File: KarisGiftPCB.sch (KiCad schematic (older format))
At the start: 43 parts

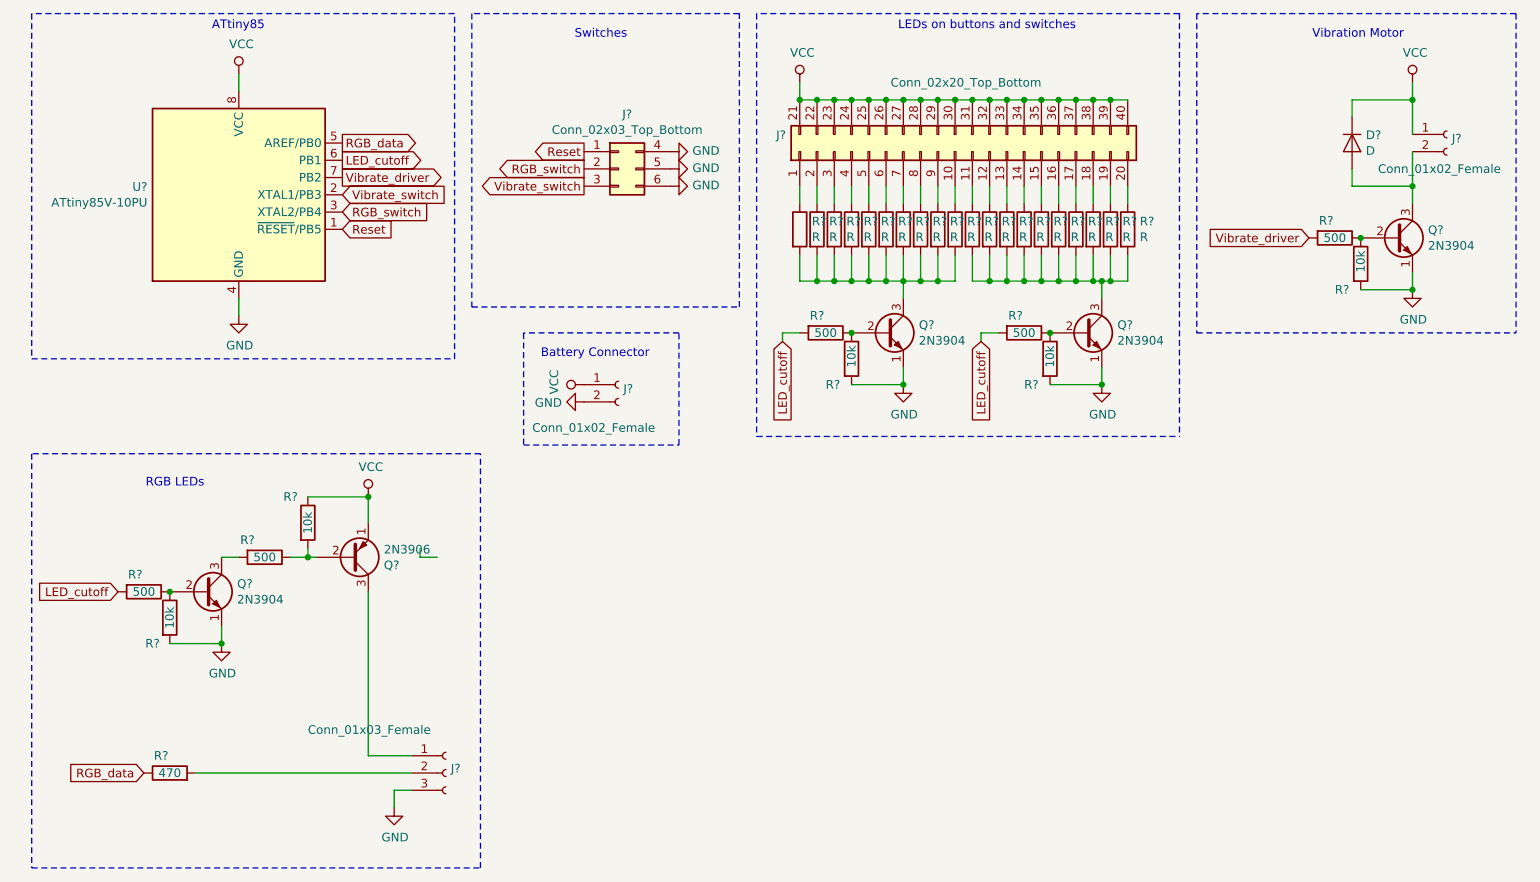
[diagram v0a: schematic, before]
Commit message: Added footprints to all parts in schematic.
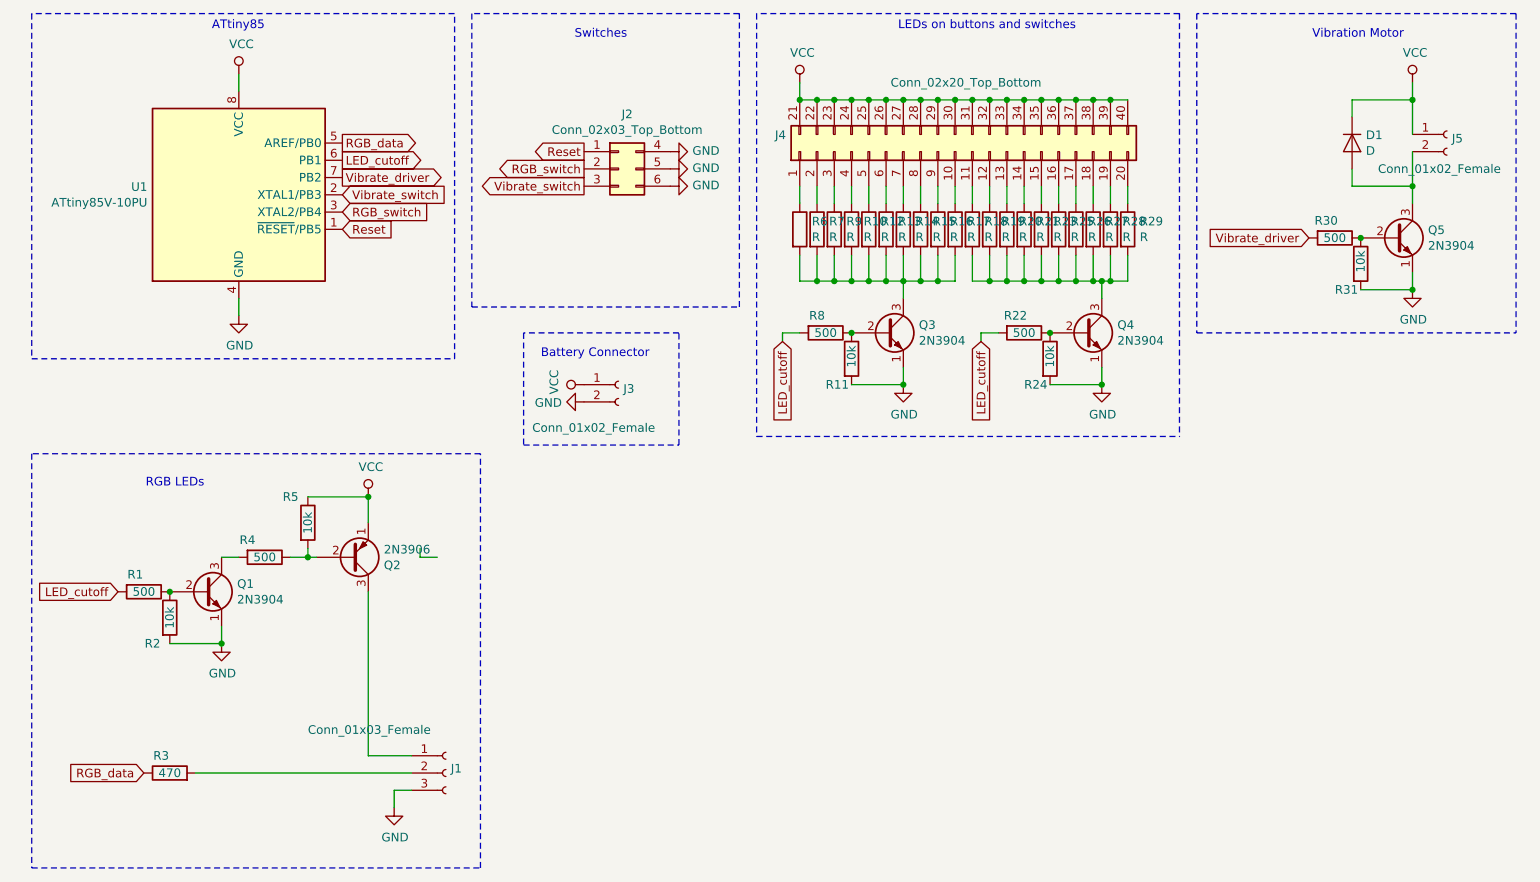
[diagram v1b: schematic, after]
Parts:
- D1: renamed from D?; footprint (none) -> Diode_THT:D_DO-41_SOD81_P10.16mm_Horizontal
- J1: renamed from J?; footprint (none) -> Connector_PinSocket_2.54mm:PinSocket_1x03_P2.54mm_Vertical
- J2: renamed from J?; footprint (none) -> Connector_PinSocket_2.54mm:PinSocket_2x03_P2.54mm_Vertical
- J3, J5: renamed from J?; footprint (none) -> Connector_PinSocket_2.54mm:PinSocket_1x02_P2.54mm_Vertical
- J4: renamed from J?; footprint (none) -> Connector_PinSocket_2.54mm:PinSocket_2x20_P2.54mm_Vertical
- R1, R10, R11, R12, R13, R14, R15, R16, R17, R18, R19, R2, R20, R21, R22, R23, R24, R25, R26, R27, R28, R29, R3, R30, R31, R4, R5, R6, R7, R8, R9: renamed from R?; footprint (none) -> Resistor_THT:R_Axial_DIN0207_L6.3mm_D2.5mm_P10.16mm_Horizontal
- gave numbers to parts that had none: 6
